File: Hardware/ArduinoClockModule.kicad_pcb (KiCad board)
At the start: 2 copper layers, 58 x 101 mm, 38 parts, among them J1 AudioJack2_SwitchT, J2 AudioJack2_SwitchT, J3 AudioJack2_SwitchT, J4 AudioJack2_SwitchT, J5 Conn_02x05_Odd_Even, SW1 SW_Push, SW2 SW_Push, SW3 RotaryEncoder_Switch, U1 LM324, U4 74HC595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

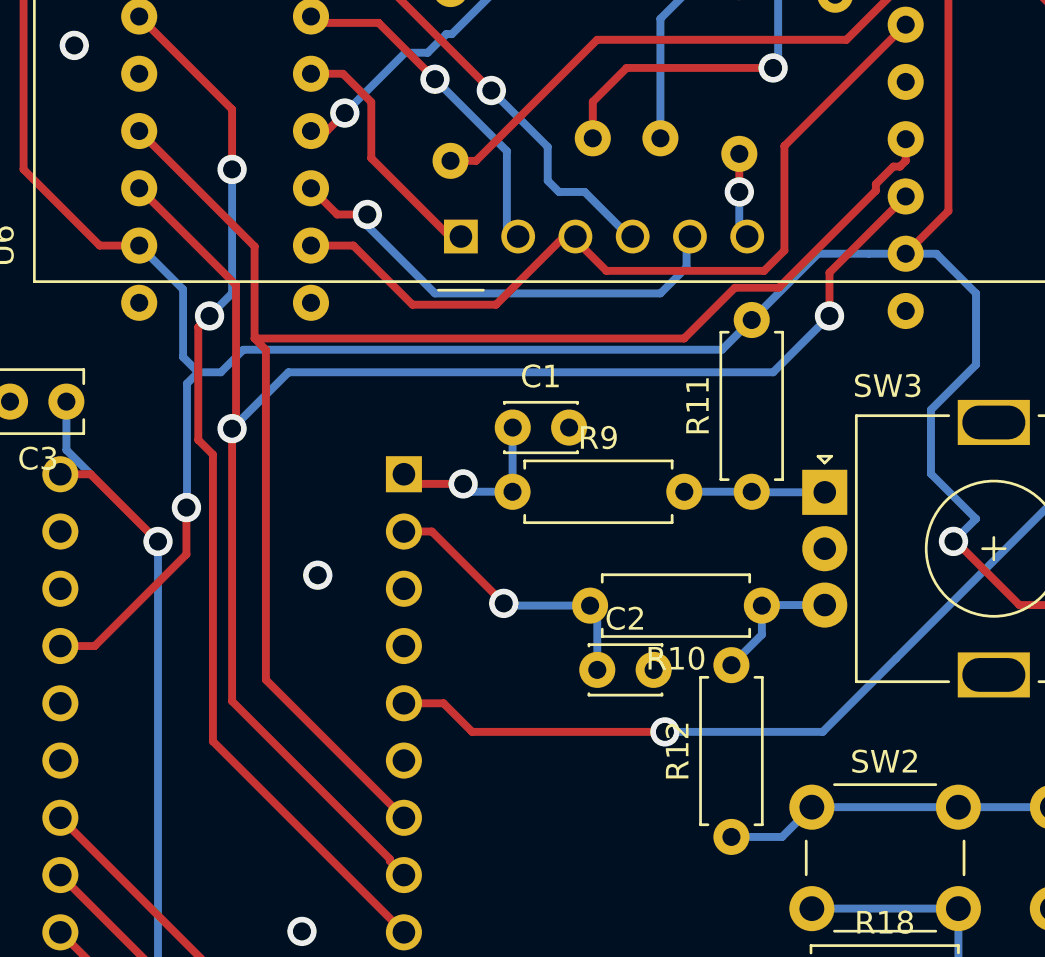
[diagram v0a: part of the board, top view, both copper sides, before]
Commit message: First working protorype. The class should allow some expansion of features wihtout too major refactors. Some modifications to the hardware is still needed.
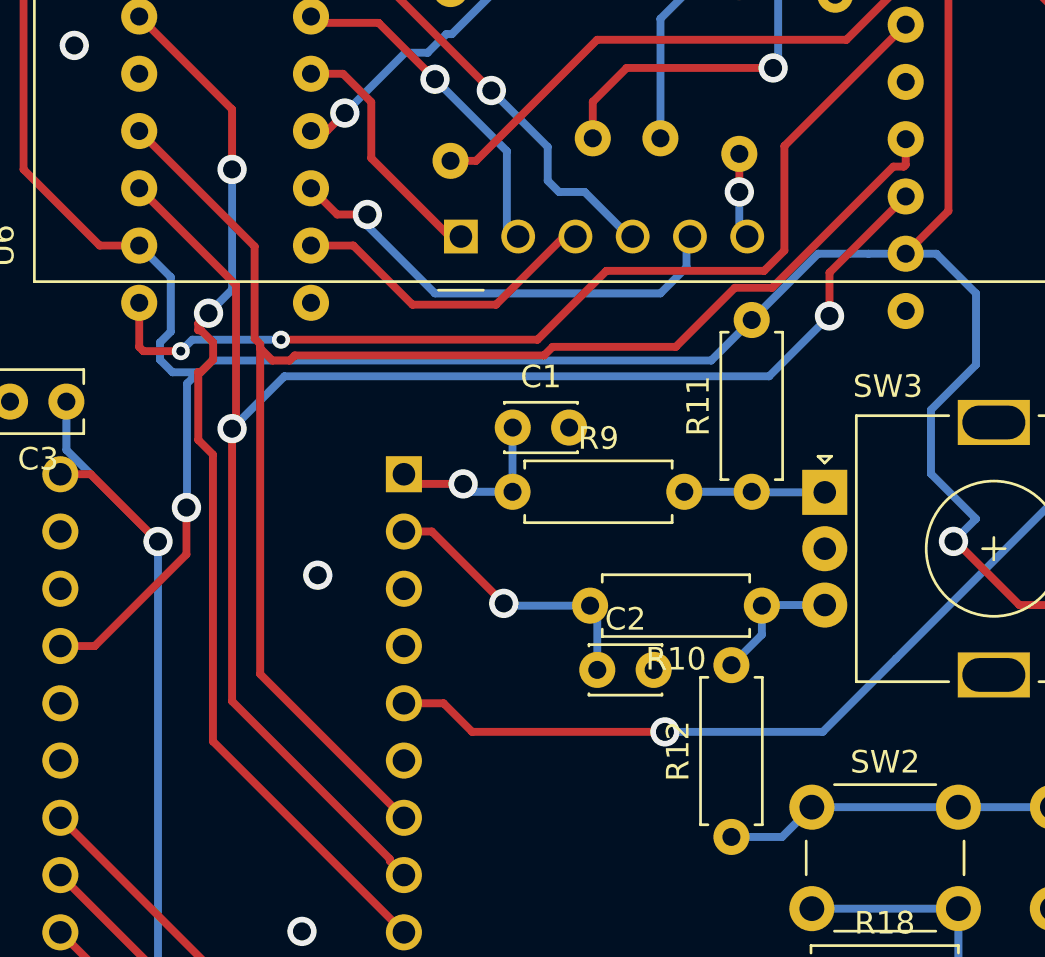
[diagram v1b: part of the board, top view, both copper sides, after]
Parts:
- R1, R2, R3, R4: value 220 -> 8k
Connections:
- U4 pad 9: unconnected-(U4-Pad9) -> Net-(U5-Pad14)
- U5 pad 14: Net-(U4-Pad7) -> Net-(U5-Pad14)
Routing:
- net Net-(U5-Pad14): track 0.00 -> 44.8 mm, vias 0 -> 2
- net Net-(U4-Pad7): track 36.6 -> 13.9 mm
- net +5V: track 156.1 -> 157.2 mm
- net /D6: track 46.7 -> 47.4 mm
- net /D4: track 68.6 -> 69.1 mm
